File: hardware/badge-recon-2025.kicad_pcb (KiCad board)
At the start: 2 copper layers, 70 parts, among them P1 USB_C_Plug_USB2.0, Q1 DMG3415U-7, SW1 SW_Push, SW2 SW_Push, SW3 ON, SW4 SOURCE MAG, SW5 SW_Push, SW6 SW_Push, SW7 RESET, U1 PN7150B0HN_C11002E-PN7150B0HN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, U2 RP2040, U4 AP2112K-3.3, U6 W25Q16JV, U7 TC4424, Y1 27.12Mhz, Y2 12Mhz

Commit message: feat(Hw):Init_Floorplan
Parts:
- added J3: Battery, Footprints:BAT-TH_BH-AAA-A1AJ024, F.Cu at (129.2, 120.6)
- added J5: OLED, Footprints:Display OLED 128 x32, F.Cu at (171.0, 80.6)
- added Ref**: Val**, Footprints:DISEÑO_BADGE RECON_2025_CONTORNO-01, F.Cu at (152.7, 95.2)
- moved C22 146.7 mm to (159.1, -73.8)
- moved C29 146.7 mm to (159.1, -56.3)
- moved C33 146.7 mm to (163.1, -73.8)
- moved D4 146.7 mm to (168.5, -43.5)
- moved F1 146.7 mm to (171.3, -59.4)
- moved Q1 146.7 mm to (171.5, -63.0)
- moved R14 146.7 mm to (163.1, -51.2)
- moved R20 146.7 mm to (167.1, -63.8)
- moved R4 146.7 mm to (163.1, -61.3)
- moved R5 146.7 mm to (163.1, -58.8)
- moved U4 146.7 mm to (171.7, -72.7)
- moved SW3 126.9 mm to (203.8, -51.8)
- moved SW1 123.9 mm to (116.6, -56.6)
- moved SW2 123.9 mm to (116.6, -49.6)
- moved SW5 123.9 mm to (116.6, -42.5)
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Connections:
- U1 pad 40: /CLK -> unconnected-(U1-CLK_REQ-Pad40)
- U2 pad 28: /GPIO1 -> unconnected-(U2-GPIO17-Pad28)
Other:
- board outline added: 78.1 x 100 mm

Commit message: feat(Hw):Update_Floorplan
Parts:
- removed Ref**: Val**, Footprints:DISEÑO_BADGE RECON_2025_CONTORNO-01
- C1, C10, C12, C13, C14, C15, C16, C17, C18, C19, C2, C20, C21, C22, C23, C24, C25, C26, C27, C28, C29, C3, C30, C31, C33, C34, C4, C5, C6, C7, C8, C9, D4, F1, J3, JP1, L1, L2, L3, L4, P1, Q1, R1, R10, R14, R15, R16, R18, R19, R2, R20, R21, R22, R3, R4, R5, R9, SW3, SW4, SW7, U1, U2, U4, U6, U7, Y1, Y2: moved to B.Cu
- moved SW1 199.3 mm to (134.8, 141.8), turned to 180 degrees
- moved SW2 193.8 mm to (147.2, 141.8), turned to 180 degrees
- moved SW3 193.6 mm to (117.5, 121.5), turned to 90 degrees
- moved U4 193.5 mm to (119.9, 113.7)
- moved C22 192.3 mm to (116.7, 113.8), turned to 90 degrees
- moved SW5 189.3 mm to (159.6, 141.8), turned to 180 degrees
- moved SW6 185.8 mm to (172.0, 141.8), turned to 180 degrees
- moved Q1 184.6 mm to (185.2, 121.0), turned to 180 degrees
- moved C33 175.1 mm to (163.0, 101.3), turned to -90 degrees
- moved C29 173.8 mm to (122.9, 113.7), turned to 90 degrees
- moved R14 170.9 mm to (187.9, 117.9), turned to 180 degrees
- moved D4 165.7 mm to (188.7, 121.0), turned to 90 degrees
- moved R20 165.1 mm to (164.5, 101.3), turned to -90 degrees
- moved F1 158.8 mm to (179.1, 99.2)
- moved R5 157.2 mm to (179.3, 97.6)
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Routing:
- net /D+: track 0.00 -> 24.8 mm
- net /D-: track 0.00 -> 24.8 mm
- net /RD+: track 0.00 -> 2.35 mm
- net /RD-: track 0.00 -> 2.35 mm

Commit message: feat(Hw):Update_BOM
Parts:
- F1: value 0.5A -> 0.75A; footprint Fuse:Fuse_0805_2012Metric -> Fuse:Fuse_0603_1608Metric
- SW3: footprint Footprints:JS102011SAQN -> Footprints:MSK12C02
- moved SW3 1.62 mm to (116.0, 121.0)

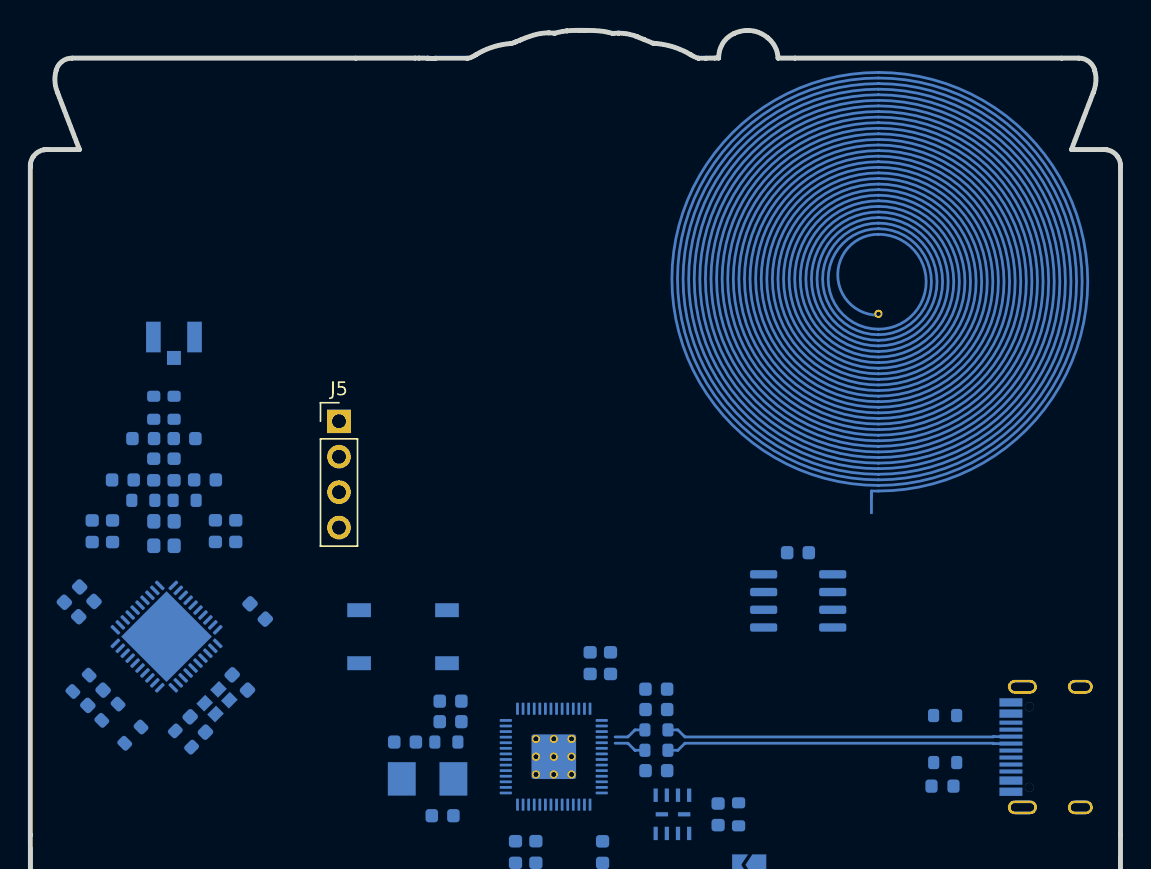
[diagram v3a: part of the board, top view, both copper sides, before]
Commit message: feat(Hw): add antenna missing matching circuit
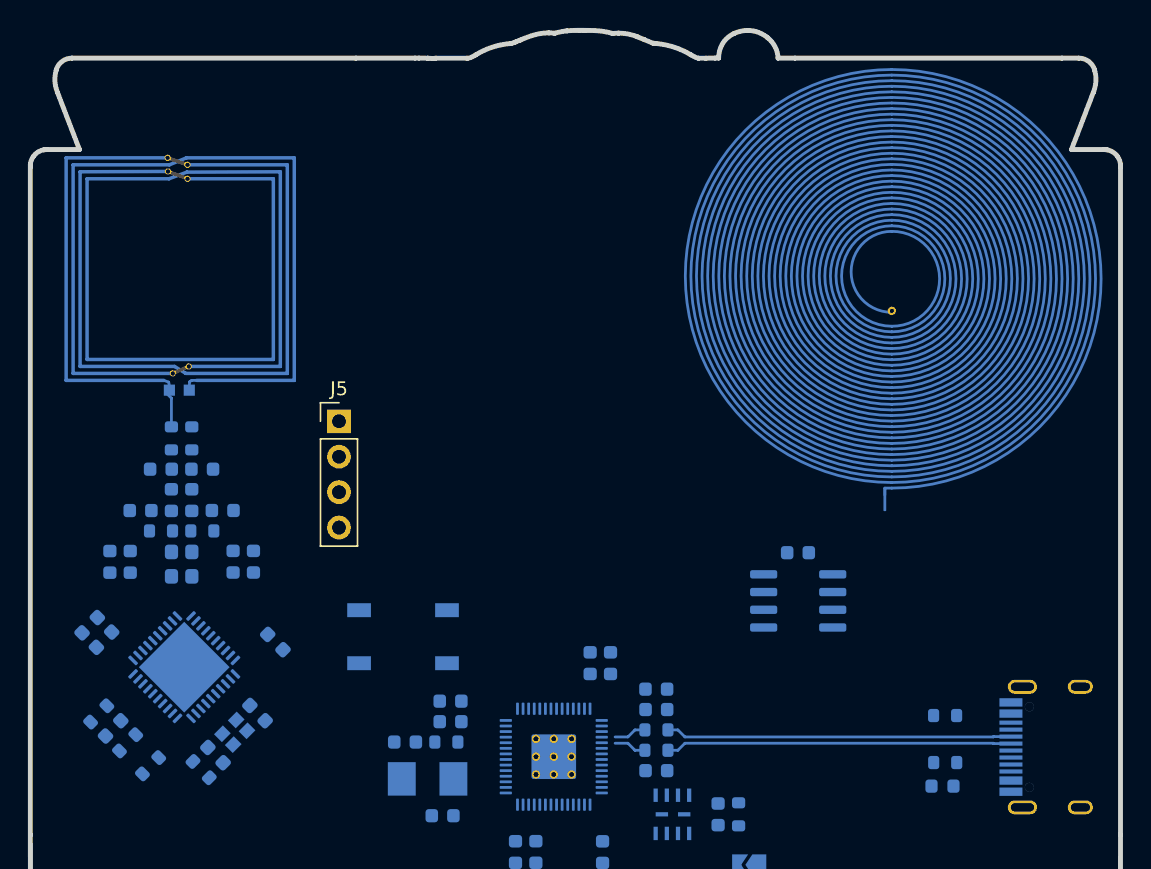
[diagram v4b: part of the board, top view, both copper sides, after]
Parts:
- L3: footprint Connectors:MOLEX_1661 -> Footprints:NFC_Antenna_4T_Crossover_Final
- moved L3 9.17 mm to (132.6, 70.2), turned to 90 degrees
- moved C23 2.53 mm to (128.2, 83.2)
- moved Y1 2.53 mm to (128.3, 95.4)
- moved C15 2.53 mm to (119.0, 88.8)
- moved C24 2.53 mm to (120.9, 83.2)
- moved C25 2.53 mm to (127.5, 79.5)
- moved C26 2.53 mm to (121.6, 79.5)
- moved C27 2.53 mm to (125.3, 78.7)
- moved C28 2.53 mm to (123.8, 78.7)
- moved C3 2.53 mm to (127.0, 97.0)
- moved C30 2.53 mm to (126.0, 76.5)
- moved C31 2.53 mm to (123.1, 76.5)
- moved C4 2.53 mm to (130.0, 94.0)
- moved C5 2.53 mm to (131.3, 88.9)
- moved C6 2.53 mm to (129.7, 83.2)
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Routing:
- net Net-(L3-Pad2): track 0.00 -> 2.50 mm

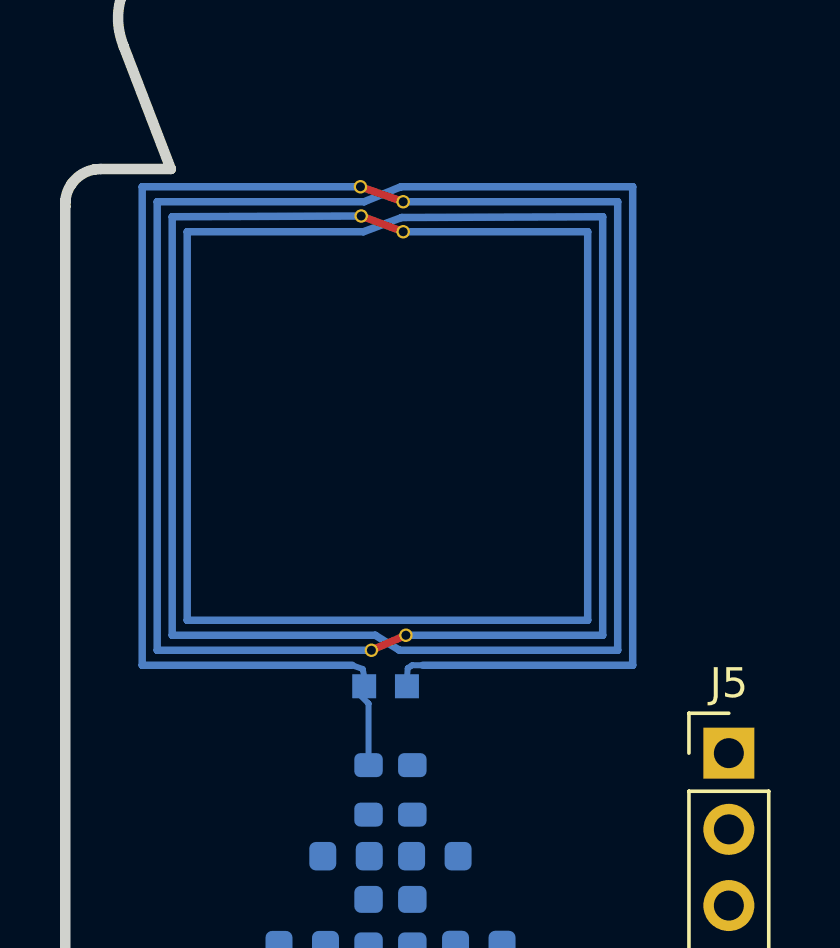
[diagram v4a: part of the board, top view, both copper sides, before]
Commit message: feat(Hw): add ideal matching circuit
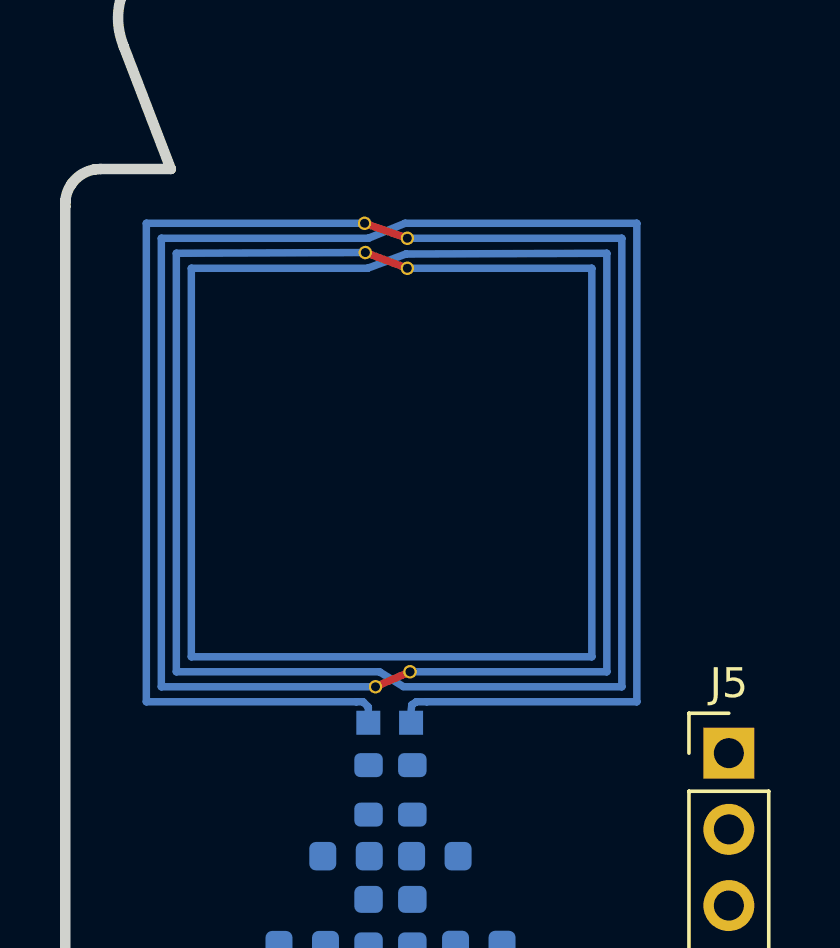
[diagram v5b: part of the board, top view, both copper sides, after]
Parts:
- moved L3 1.23 mm to (132.8, 71.4)
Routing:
- net Net-(L3-Pad2): track 2.50 -> 0.00 mm
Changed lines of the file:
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@@
 	(footprint "Footprints:NFC_Antenna_4T_Crossover_Final"
 		(layer "B.Cu")
-		(at 132.615 70.17 90)
+		(at 132.7525 71.3875 90)
 		(property "Reference" "L3"
 			(at 3 1 270)
@@
 		(fp_line
 			(start 0 -9.35)
-			(end -0.125 -9)
+			(end 0 -9.125)
 			(stroke
-				(width 0.2)
-				(type default)
+				(width 0.25)
+				(type solid)
 			)
 			(layer "B.Cu")
 		)
 		(fp_line
-			(start 15.95 -9.075)
-			(end 15.95 -16.35)
+			(start 0 -9.125)
+			(end -0.175 -8.95)
 			(stroke
 				(width 0.25)
@@
 		)
 		(fp_line
-			(start 14.975 -9.05)
-			(end 14.95 -15.35)
+			(start 15.95 -9.075)
+			(end 15.95 -16.35)
 			(stroke
 				(width 0.25)
@@
 		)
 		(fp_line
-			(start -0.125 -9)
-			(end -0.625 -8.9)
+			(start 14.975 -9.05)
+			(end 14.95 -15.35)
 			(stroke
-				(width 0.2)
+				(width 0.25)
 				(type solid)
 			)
@@
 		)
 		(fp_line
+			(start -0.175 -8.95)
+			(end -0.425 -8.95)
+			(stroke
+				(width 0.25)
+				(type solid)
+			)
+			(layer "B.Cu")
+		)
+		(fp_line
 			(start 0.51 -7.79)
 			(end 1 -8.58)
@@
 		(fp_line
 			(start -0.1 -7.5)
-			(end -0.775 -7.55)
+			(end -0.3 -7.525)
 			(stroke
-				(width 0.2)
-				(type default)
+				(width 0.25)
+				(type solid)
 			)
 			(layer "B.Cu")
@@
 			(end -0.1 -7.5)
 			(stroke
-				(width 0.2)
-				(type default)
+				(width 0.25)
+				(type solid)
 			)
 			(layer "B.Cu")
@@
 			(end 0 -7.35)
 			(stroke
-				(width 0.2)
-				(type default)
+				(width 0.25)
+				(type solid)
 			)
 			(layer "B.Cu")
@@
 		(net 36)
 	)
-	(segment
-		(start 123.809688 73.499563)
-		(end 123.809688 71.445775)
-		(width 0.2)
-		(layer "B.Cu")
-		(net 38)
-	)
-	(segment
-		(start 123.809688 71.445775)
-		(end 123.492565 71.128652)
-		(width 0.2)
-		(layer "B.Cu")
-		(net 38)
-	)
 	(group ""

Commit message: Feat(Hw): floorplan added
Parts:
- C25, C26: value 680pF -> 252.8pF
- C27, C28: value 100pF/50V -> 63.3pF/50V
- C30, C31: value 120pF -> 813.5pF
- L1, L2: value 160nH -> 470nH
- R18, R19: value 3.24R -> 0.39R
- moved L3 7.97 mm to (134.1, 63.5)
- moved C28 6.79 mm to (125.1, 72.1)
- moved C6 6.79 mm to (131.0, 76.5)
- moved R19 6.79 mm to (125.1, 67.7)
- moved C24 6.79 mm to (122.2, 76.5)
- moved C26 6.79 mm to (122.9, 72.8)
- moved C27 6.79 mm to (126.6, 72.1)
- moved C30 6.79 mm to (127.3, 69.9)
- moved C31 6.79 mm to (124.4, 69.9)
- moved C7 6.79 mm to (120.7, 76.5)
- moved L1 6.79 mm to (126.6, 76.7)
- moved L2 6.79 mm to (125.1, 76.7)
- moved R15 6.79 mm to (127.3, 74.3)
- moved R16 6.79 mm to (124.4, 74.3)
- moved R18 6.79 mm to (126.6, 67.7)
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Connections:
- P1 pad S1: unconnected-(P1-SHIELD-PadS1)_1 -> GND
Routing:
- net GND: track 0.00 -> 26.7 mm, vias 0 -> 3
- net /OUTB: track 0.00 -> 20.0 mm, vias 0 -> 1
- net /RXP: track 0.00 -> 15.6 mm, vias 0 -> 2
- net +3V3: track 0.00 -> 14.6 mm
- net Net-(F1-Pad1): track 0.00 -> 14.0 mm
- net +1V2: track 0.00 -> 7.27 mm
- net Net-(U1-VDD): track 0.00 -> 6.68 mm
- net /RXN: track 0.00 -> 6.57 mm
- net Net-(U1-VDD(TX)): track 0.00 -> 6.46 mm, vias 0 -> 1
- net /BUTTON_3: track 0.00 -> 6.30 mm
- net /BUTTON_2: track 0.00 -> 6.30 mm
- net /BUTTON_1: track 0.00 -> 6.30 mm
- net /BUTTON_4: track 0.00 -> 6.30 mm
- net Net-(U1-NFC_CLK_XTAL1): track 0.00 -> 5.54 mm
- net /TX2: track 0.00 -> 5.42 mm
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- added copper zone on B.Cu, net GND
- added copper zone on F.Cu, net GND
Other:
- outline, holes or cut-outs redrawn
- board text added: "- Check PN7150 crystal - Change flash memmory packaging - Check switch avaaiability - Check RP2040 crystal - Check fuse"
